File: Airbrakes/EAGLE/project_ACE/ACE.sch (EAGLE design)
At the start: 4 parts, among them J3 PTH

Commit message: Update ACE.sch
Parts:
- added 0OHM: (no value), fab_new:R1206
- added PAD1, PAD2: (no value), wirepad:2,15/1,0
- added POWER_TERMINAL: CONN_02_TERM-ADAFRUIT, fab_new:CONN_02_TERM-ADAFRUIT
- added R1, R2: 0 ohm, fab_new:R1206
- added SERVO_TERMINAL: CONN_03_TERM'-FABLAB', fab_new:CONN_03_TERM'-FABLAB'
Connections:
- new net 7.4V: POWER_TERMINAL.2, SERVO_TERMINAL.3
- new net N$2: R1.2, R2.1
- new net PWM: 0OHM.1, 0OHM.2, SERVO_TERMINAL.1, U$10.PWM_7
- net GND: now also PAD1.P, PAD2.P, POWER_TERMINAL.1, R2.2, SERVO_TERMINAL.2
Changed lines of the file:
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@@
 <layers>
 <layer number="1" name="Top" color="4" fill="1" visible="no" active="no"/>
+<layer number="2" name="Route2" color="1" fill="3" visible="no" active="no"/>
+<layer number="3" name="Route3" color="4" fill="3" visible="no" active="no"/>
+<layer number="4" name="Route4" color="1" fill="4" visible="no" active="no"/>
+<layer number="5" name="Route5" color="4" fill="4" visible="no" active="no"/>
+<layer number="6" name="Route6" color="1" fill="8" visible="no" active="no"/>
+<layer number="7" name="Route7" color="4" fill="8" visible="no" active="no"/>
+<layer number="8" name="Route8" color="1" fill="2" visible="no" active="no"/>
+<layer number="9" name="Route9" color="4" fill="2" visible="no" active="no"/>
+<layer number="10" name="Route10" color="1" fill="7" visible="no" active="no"/>
+<layer number="11" name="Route11" color="4" fill="7" visible="no" active="no"/>
+<layer number="12" name="Route12" color="1" fill="5" visible="no" active="no"/>
+<layer number="13" name="Route13" color="4" fill="5" visible="no" active="no"/>
+<layer number="14" name="Route14" color="1" fill="6" visible="no" active="no"/>
+<layer number="15" name="Route15" color="4" fill="6" visible="no" active="no"/>
 <layer number="16" name="Bottom" color="1" fill="1" visible="no" active="no"/>
 <layer number="17" name="Pads" color="2" fill="1" visible="no" active="no"/>
@@
 <part name="P+1" library="supply1" library_urn="urn:adsk.eagle:library:371" deviceset="VCC" device=""/>
 <part name="U$12" library="microbuilder" deviceset="GND" device=""/>
+<part name="R1" library="fab_new" deviceset="R" device="1206" value="0 ohm"/>
+<part name="R2" library="fab_new" deviceset="R" device="1206" value="0 ohm"/>
+<part name="POWER_TERMINAL" library="fab_new" deviceset="CONN_02_TERM" device="-ADAFRUIT"/>
+<part name="SERVO_TERMINAL" library="fab_new" deviceset="CONN_03_TERM" device="'-FABLAB'"/>
+<part name="0OHM" library="fab_new" deviceset="R" device="1206"/>
+<part name="PAD1" library="wirepad" library_urn="urn:adsk.eagle:library:412" deviceset="2,15/1,0" device="" package3d_urn="urn:adsk.eagle:package:30831/1"/>
+<part name="PAD2" library="wirepad" library_urn="urn:adsk.eagle:library:412" deviceset="2,15/1,0" device="" package3d_urn="urn:adsk.eagle:package:30831/1"/>
 </parts>
 <sheets>
@@
 <attribute name="VALUE" x="39.116" y="55.88" size="1.27" layer="96"/>
 </instance>
+<instance part="R1" gate="G$1" x="35.56" y="2.54" smashed="yes">
+<attribute name="NAME" x="31.75" y="4.0386" size="1.778" layer="95"/>
+<attribute name="VALUE" x="31.75" y="-0.762" size="1.778" layer="96"/>
+</instance>
+<instance part="R2" gate="G$1" x="45.72" y="2.54" smashed="yes">
+<attribute name="NAME" x="41.91" y="4.0386" size="1.778" layer="95"/>
+<attribute name="VALUE" x="41.91" y="-0.762" size="1.778" layer="96"/>
+</instance>
+<instance part="POWER_TERMINAL" gate="G$1" x="53.34" y="55.88" smashed="yes" rot="R90">
+<attribute name="NAME" x="47.625" y="53.34" size="1.778" layer="95" rot="R90"/>
+</instance>
+<instance part="SERVO_TERMINAL" gate="G$1" x="53.34" y="45.72" smashed="yes" rot="R90">
+<attribute name="NAME" x="47.625" y="43.18" size="1.778" layer="95" rot="R90"/>
+</instance>
+<instance part="0OHM" gate="G$1" x="-5.08" y="33.02" smashed="yes">
+<attribute name="NAME" x="-8.89" y="34.5186" size="1.778" layer="95"/>
+<attribute name="VALUE" x="-8.89" y="29.718" size="1.778" layer="96"/>
+</instance>
+<instance part="PAD1" gate="1" x="48.26" y="15.24" smashed="yes">
+<attribute name="NAME" x="47.117" y="17.0942" size="1.778" layer="95"/>
+<attribute name="VALUE" x="47.117" y="11.938" size="1.778" layer="96"/>
+</instance>
+<instance part="PAD2" gate="1" x="50.8" y="0" smashed="yes" rot="R90">
+<attribute name="NAME" x="48.9458" y="-1.143" size="1.778" layer="95" rot="R90"/>
+<attribute name="VALUE" x="54.102" y="-1.143" size="1.778" layer="96" rot="R90"/>
+</instance>
 </instances>
 <busses>
@@
 <wire x1="71.12" y1="17.78" x2="71.12" y2="15.24" width="0.1524" layer="91"/>
 <pinref part="GND12" gate="1" pin="GND"/>
+<pinref part="R2" gate="G$1" pin="2"/>
+<wire x1="71.12" y1="15.24" x2="50.8" y2="15.24" width="0.1524" layer="91"/>
+<wire x1="50.8" y1="15.24" x2="50.8" y2="2.54" width="0.1524" layer="91"/>
+<junction x="71.12" y="15.24"/>
+<pinref part="PAD1" gate="1" pin="P"/>
+<junction x="50.8" y="15.24"/>
+<pinref part="PAD2" gate="1" pin="P"/>
+<junction x="50.8" y="2.54"/>
 </segment>
 <segment>
@@
 <wire x1="35.56" y1="60.96" x2="40.64" y2="60.96" width="0.1524" layer="91"/>
 <pinref part="U$10" gate="G$1" pin="GND"/>
+<wire x1="40.64" y1="60.96" x2="40.64" y2="55.88" width="0.1524" layer="91"/>
+<junction x="40.64" y="60.96"/>
+<pinref part="POWER_TERMINAL" gate="G$1" pin="1"/>
+<wire x1="40.64" y1="55.88" x2="50.8" y2="55.88" width="0.1524" layer="91"/>
+<pinref part="SERVO_TERMINAL" gate="G$1" pin="2"/>
+<wire x1="53.34" y1="45.72" x2="53.34" y2="53.34" width="0.1524" layer="91"/>
+<wire x1="53.34" y1="53.34" x2="50.8" y2="53.34" width="0.1524" layer="91"/>
+<wire x1="50.8" y1="53.34" x2="50.8" y2="55.88" width="0.1524" layer="91"/>
+<junction x="50.8" y="55.88"/>
 </segment>
 </net>
@@
 <pinref part="U$1" gate="G$1" pin="GND_1"/>
 <wire x1="165.1" y1="53.34" x2="175.26" y2="53.34" width="0.1524" layer="91"/>
+</segment>
+</net>
+<net name="N$2" class="0">
+<segment>
+<pinref part="R1" gate="G$1" pin="2"/>
+<pinref part="R2" gate="G$1" pin="1"/>
+</segment>
+</net>
+<net name="7.4V" class="0">
+<segment>
+<pinref part="POWER_TERMINAL" gate="G$1" pin="2"/>
+<pinref part="SERVO_TERMINAL" gate="G$1" pin="3"/>
+<wire x1="53.34" y1="55.88" x2="55.88" y2="55.88" width="0.1524" layer="91"/>
+<wire x1="55.88" y1="55.88" x2="55.88" y2="45.72" width="0.1524" layer="91"/>
+</segment>
+</net>
+<net name="PWM" class="0">
+<segment>
+<pinref part="0OHM" gate="G$1" pin="1"/>
+<wire x1="-10.16" y1="33.02" x2="-10.16" y2="27.94" width="0.1524" layer="91"/>
+<wire x1="-10.16" y1="27.94" x2="0" y2="27.94" width="0.1524" layer="91"/>
+<pinref part="SERVO_TERMINAL" gate="G$1" pin="1"/>
+<wire x1="0" y1="27.94" x2="50.8" y2="27.94" width="0.1524" layer="91"/>
+<wire x1="53.34" y1="27.94" x2="50.8" y2="27.94" width="0.1524" layer="91"/>
+<wire x1="50.8" y1="27.94" x2="50.8" y2="45.72" width="0.1524" layer="91"/>
+<pinref part="U$10" gate="G$1" pin="PWM_7"/>
+<pinref part="0OHM" gate="G$1" pin="2"/>
+<wire x1="0" y1="33.02" x2="0" y2="27.94" width="0.1524" layer="91"/>
+<junction x="0" y="33.02"/>
+<junction x="0" y="27.94"/>
 </segment>
 </net>
@@
 will not be understood (or retained) with this version.
 </note>
+<note version="8.3" severity="warning">
+Since Version 8.3, EAGLE supports the association of 3D packages
+with devices in libraries, schematics, and board files. Those 3D
+packages will not be understood (or retained) with this version.
+</note>
 </compatibility>

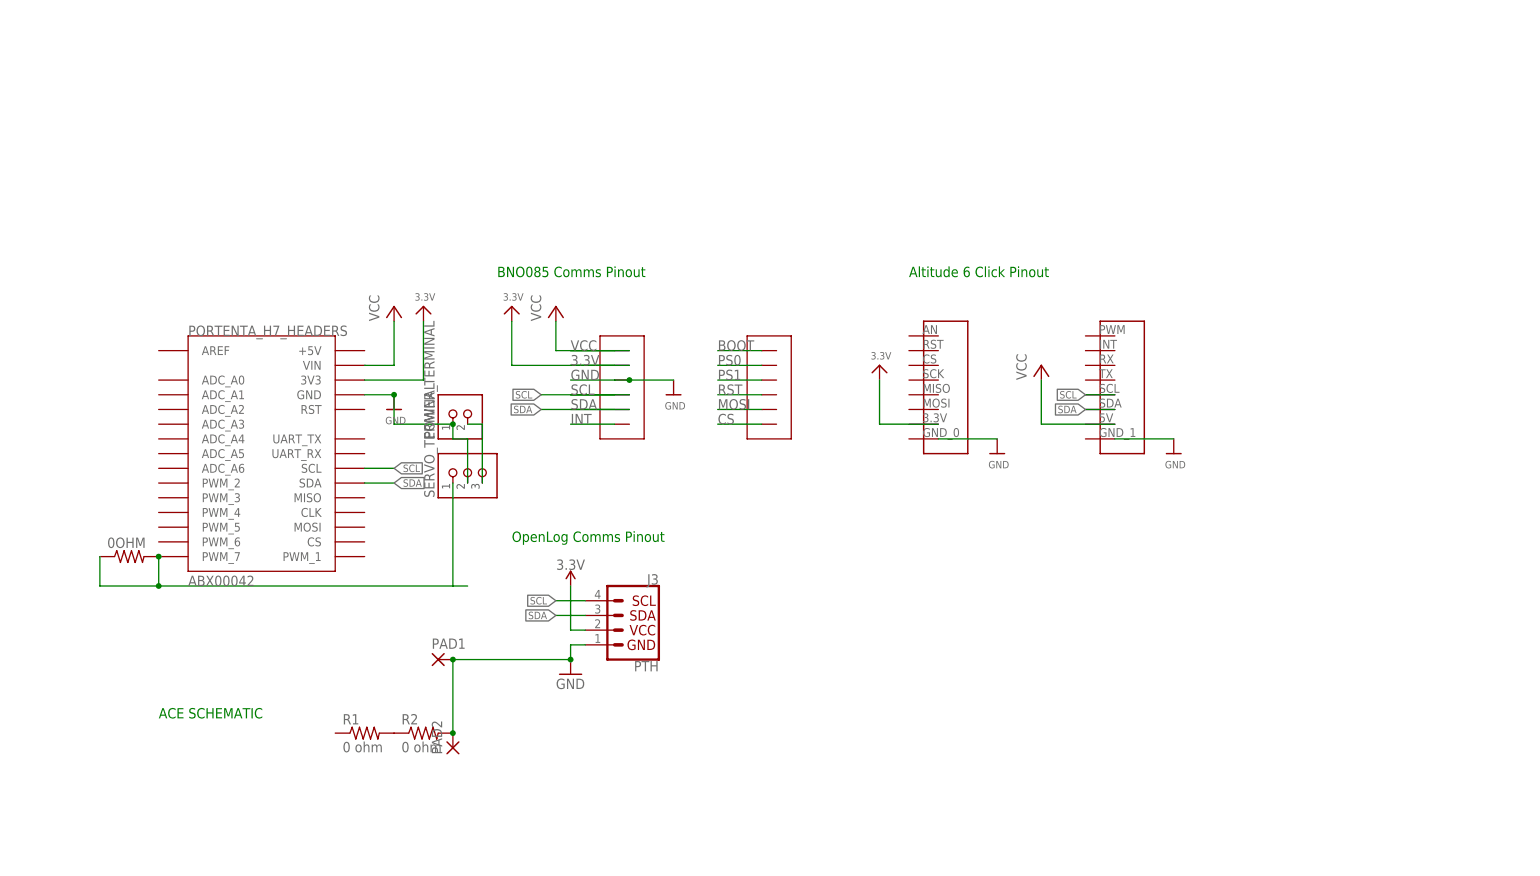
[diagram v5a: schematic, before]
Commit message: Reroute layout and schematic
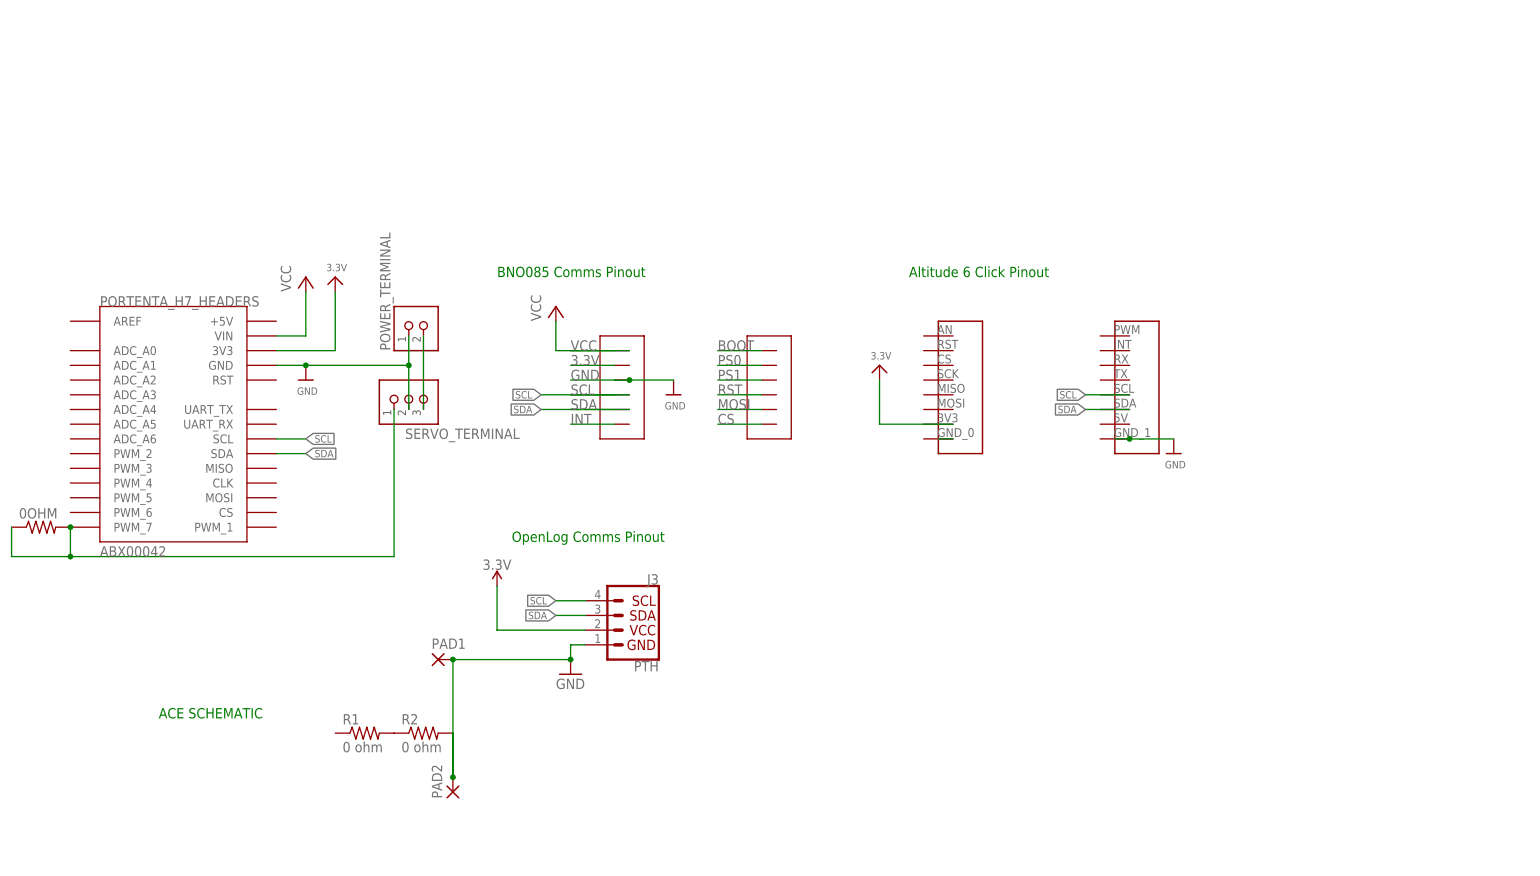
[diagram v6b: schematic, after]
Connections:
- removed net N$1: U$1.GND_1
- new net N$4: U$1.GND_0
- net 3.3V: no longer U$5.3.3V
- net GND: now also U$1.GND_1; no longer U$1.GND_0
- net VCC: no longer U$1.5V
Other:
- moved on the sheet: 0OHM, PAD2, POWER_TERMINAL, SERVO_TERMINAL

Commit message: ACE PCB updates
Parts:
- removed PAD1, PAD2: (no value), wirepad:2,15/1,0
- removed R1, R2: 0 ohm, fab_new:R1206
- added ROTARY_TERMINAL: CONN_02_TERM-ADAFRUIT, fab_new:CONN_02_TERM-ADAFRUIT
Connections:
- removed net N$2: R1.2, R2.1
- net GND: now also ROTARY_TERMINAL.1, ROTARY_TERMINAL.2; no longer PAD1.P, PAD2.P, R2.2
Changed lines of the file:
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@@
 <part name="P+1" library="supply1" library_urn="urn:adsk.eagle:library:371" deviceset="VCC" device=""/>
 <part name="U$12" library="microbuilder" deviceset="GND" device=""/>
-<part name="R1" library="fab_new" deviceset="R" device="1206" value="0 ohm"/>
-<part name="R2" library="fab_new" deviceset="R" device="1206" value="0 ohm"/>
 <part name="POWER_TERMINAL" library="fab_new" deviceset="CONN_02_TERM" device="-ADAFRUIT"/>
 <part name="SERVO_TERMINAL" library="fab_new" deviceset="CONN_03_TERM" device="'-FABLAB'"/>
 <part name="0OHM" library="fab_new" deviceset="R" device="1206"/>
-<part name="PAD1" library="wirepad" library_urn="urn:adsk.eagle:library:412" deviceset="2,15/1,0" device="" package3d_urn="urn:adsk.eagle:package:30831/1"/>
-<part name="PAD2" library="wirepad" library_urn="urn:adsk.eagle:library:412" deviceset="2,15/1,0" device="" package3d_urn="urn:adsk.eagle:package:30831/1"/>
 <part name="U$1" library="MIKROE-4903" deviceset="MIKROE-ALTITUDE-6-CLICK-DVC" device=""/>
+<part name="ROTARY_TERMINAL" library="fab_new" deviceset="CONN_02_TERM" device="-ADAFRUIT"/>
 </parts>
 <sheets>
@@
 <attribute name="VALUE" x="23.876" y="60.96" size="1.27" layer="96"/>
 </instance>
-<instance part="R1" gate="G$1" x="35.56" y="2.54" smashed="yes">
-<attribute name="NAME" x="31.75" y="4.0386" size="1.778" layer="95"/>
-<attribute name="VALUE" x="31.75" y="-0.762" size="1.778" layer="96"/>
-</instance>
-<instance part="R2" gate="G$1" x="45.72" y="2.54" smashed="yes">
-<attribute name="NAME" x="41.91" y="4.0386" size="1.778" layer="95"/>
-<attribute name="VALUE" x="41.91" y="-0.762" size="1.778" layer="96"/>
-</instance>
 <instance part="POWER_TERMINAL" gate="G$1" x="45.72" y="71.12" smashed="yes" rot="R90">
 <attribute name="NAME" x="40.005" y="68.58" size="1.778" layer="95" rot="R90"/>
@@
 <attribute name="VALUE" x="-24.13" y="34.798" size="1.778" layer="96"/>
 </instance>
-<instance part="PAD1" gate="1" x="48.26" y="15.24" smashed="yes">
-<attribute name="NAME" x="47.117" y="17.0942" size="1.778" layer="95"/>
-<attribute name="VALUE" x="47.117" y="11.938" size="1.778" layer="96"/>
-</instance>
-<instance part="PAD2" gate="1" x="50.8" y="-7.62" smashed="yes" rot="R90">
-<attribute name="NAME" x="48.9458" y="-8.763" size="1.778" layer="95" rot="R90"/>
-<attribute name="VALUE" x="54.102" y="-8.763" size="1.778" layer="96" rot="R90"/>
-</instance>
 <instance part="U$1" gate="G$1" x="134.62" y="50.8" smashed="yes"/>
+<instance part="ROTARY_TERMINAL" gate="G$1" x="68.58" y="2.54" smashed="yes" rot="R270">
+<attribute name="NAME" x="74.295" y="5.08" size="1.778" layer="95" rot="R270"/>
+</instance>
 </instances>
 <busses>
@@
 <wire x1="71.12" y1="17.78" x2="71.12" y2="15.24" width="0.1524" layer="91"/>
 <pinref part="GND12" gate="1" pin="GND"/>
-<pinref part="R2" gate="G$1" pin="2"/>
-<wire x1="71.12" y1="15.24" x2="50.8" y2="15.24" width="0.1524" layer="91"/>
-<wire x1="50.8" y1="15.24" x2="50.8" y2="-5.08" width="0.1524" layer="91"/>
+<pinref part="ROTARY_TERMINAL" gate="G$1" pin="2"/>
+<pinref part="ROTARY_TERMINAL" gate="G$1" pin="1"/>
+<wire x1="68.58" y1="2.54" x2="71.12" y2="2.54" width="0.1524" layer="91"/>
+<wire x1="71.12" y1="15.24" x2="71.12" y2="2.54" width="0.1524" layer="91"/>
 <junction x="71.12" y="15.24"/>
-<pinref part="PAD1" gate="1" pin="P"/>
-<junction x="50.8" y="15.24"/>
-<pinref part="PAD2" gate="1" pin="P"/>
-<junction x="50.8" y="-5.08"/>
-<wire x1="50.8" y1="-5.08" x2="50.8" y2="2.54" width="0.1524" layer="91"/>
+<junction x="71.12" y="2.54"/>
 </segment>
 <segment>
@@
 <label x="25.4" y="50.8" size="1.27" layer="95" xref="yes"/>
 <pinref part="U$10" gate="G$1" pin="SDA"/>
-</segment>
-</net>
-<net name="N$2" class="0">
-<segment>
-<pinref part="R1" gate="G$1" pin="2"/>
-<pinref part="R2" gate="G$1" pin="1"/>
 </segment>
 </net>
@@
 will not be understood (or retained) with this version.
 </note>
-<note version="8.3" severity="warning">
-Since Version 8.3, EAGLE supports the association of 3D packages
-with devices in libraries, schematics, and board files. Those 3D
-packages will not be understood (or retained) with this version.
-</note>
 </compatibility>

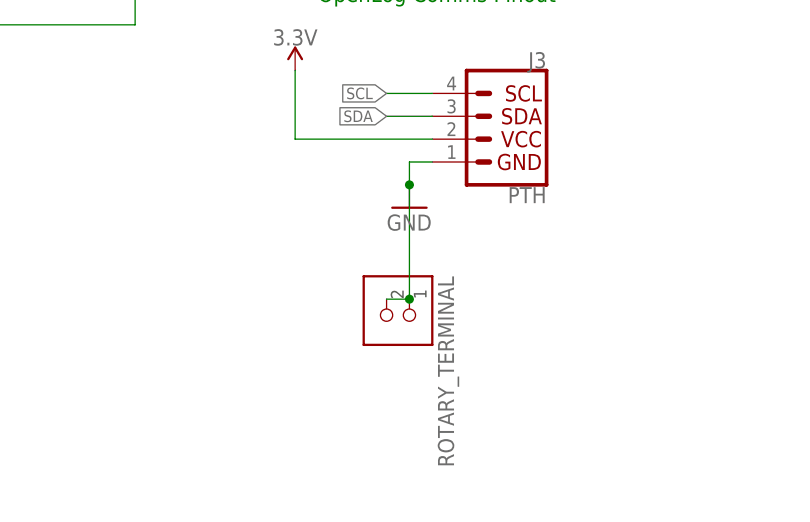
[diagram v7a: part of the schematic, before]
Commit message: change terminals on ACE PCB to 200mil pitch
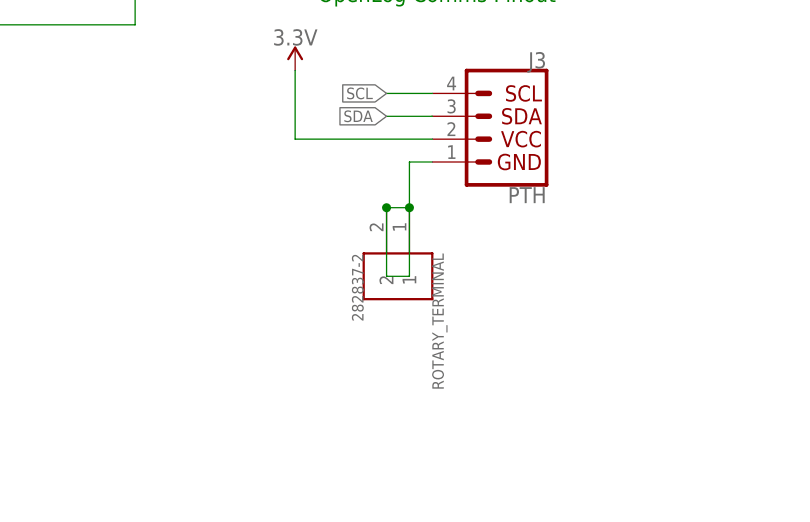
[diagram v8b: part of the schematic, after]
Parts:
- ROTARY_TERMINAL: value CONN_02_TERM-ADAFRUIT -> 282837-2; device fab_new:CONN_02_TERM-ADAFRUIT -> 282837-2:282837-2
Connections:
- new net N$2: J3.GND, ROTARY_TERMINAL.1, ROTARY_TERMINAL.2
- net GND: no longer J3.GND, ROTARY_TERMINAL.1, ROTARY_TERMINAL.2
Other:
- moved on the sheet: ROTARY_TERMINAL
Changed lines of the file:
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@@
 <part name="SUPPLY7" library="SparkFun-PowerSymbols" deviceset="3.3V" device=""/>
 <part name="J3" library="SparkX" deviceset="I2C_STANDARD" device="_NO_SILK" value="PTH"/>
-<part name="GND12" library="SparkFun" deviceset="GND" device=""/>
 <part name="U$3" library="microbuilder" deviceset="GND" device=""/>
 <part name="U$4" library="microbuilder" deviceset="3.3V" device=""/>
@@
 <part name="0OHM" library="fab_new" deviceset="R" device="1206"/>
 <part name="U$1" library="MIKROE-4903" deviceset="MIKROE-ALTITUDE-6-CLICK-DVC" device=""/>
-<part name="ROTARY_TERMINAL" library="fab_new" deviceset="CONN_02_TERM" device="-ADAFRUIT"/>
+<part name="ROTARY_TERMINAL" library="282837-2" deviceset="282837-2" device=""/>
 </parts>
 <sheets>
@@
 <attribute name="NAME" x="86.36" y="28.194" size="1.778" layer="95" font="vector" rot="MR0"/>
 </instance>
-<instance part="GND12" gate="1" x="71.12" y="12.7" smashed="yes">
-<attribute name="VALUE" x="68.58" y="10.16" size="1.778" layer="96"/>
-</instance>
 <instance part="U$3" gate="G$1" x="175.26" y="50.8" smashed="yes">
 <attribute name="VALUE" x="173.736" y="48.26" size="1.27" layer="96"/>
@@
 </instance>
 <instance part="U$1" gate="G$1" x="134.62" y="50.8" smashed="yes"/>
-<instance part="ROTARY_TERMINAL" gate="G$1" x="68.58" y="2.54" smashed="yes" rot="R270">
-<attribute name="NAME" x="74.295" y="5.08" size="1.778" layer="95" rot="R270"/>
+<instance part="ROTARY_TERMINAL" gate="G$1" x="71.12" y="5.08" smashed="yes" rot="R270">
+<attribute name="NAME" x="73.66381875" y="7.620559375" size="1.271909375" layer="95" rot="R270"/>
+<attribute name="VALUE" x="64.745490625" y="7.62236875" size="1.274909375" layer="96" rot="R270"/>
 </instance>
 </instances>
@@
 <nets>
 <net name="GND" class="2">
-<segment>
-<pinref part="J3" gate="G$1" pin="GND"/>
-<wire x1="73.66" y1="17.78" x2="71.12" y2="17.78" width="0.1524" layer="91"/>
-<wire x1="71.12" y1="17.78" x2="71.12" y2="15.24" width="0.1524" layer="91"/>
-<pinref part="GND12" gate="1" pin="GND"/>
-<pinref part="ROTARY_TERMINAL" gate="G$1" pin="2"/>
-<pinref part="ROTARY_TERMINAL" gate="G$1" pin="1"/>
-<wire x1="68.58" y1="2.54" x2="71.12" y2="2.54" width="0.1524" layer="91"/>
-<wire x1="71.12" y1="15.24" x2="71.12" y2="2.54" width="0.1524" layer="91"/>
-<junction x="71.12" y="15.24"/>
-<junction x="71.12" y="2.54"/>
-</segment>
 <segment>
 <pinref part="U$7" gate="G$1" pin="GND"/>
@@
 </segment>
 </net>
+<net name="N$2" class="2">
+<segment>
+<pinref part="J3" gate="G$1" pin="GND"/>
+<wire x1="73.66" y1="17.78" x2="71.12" y2="17.78" width="0.1524" layer="91"/>
+<pinref part="ROTARY_TERMINAL" gate="G$1" pin="1"/>
+<wire x1="71.12" y1="17.78" x2="71.12" y2="12.7" width="0.1524" layer="91"/>
+<pinref part="ROTARY_TERMINAL" gate="G$1" pin="2"/>
+<wire x1="71.12" y1="12.7" x2="68.58" y2="12.7" width="0.1524" layer="91"/>
+<junction x="71.12" y="12.7"/>
+<wire x1="71.12" y1="12.7" x2="71.12" y2="5.08" width="0.1524" layer="91"/>
+<wire x1="71.12" y1="5.08" x2="68.58" y2="5.08" width="0.1524" layer="91"/>
+<wire x1="68.58" y1="5.08" x2="68.58" y2="12.7" width="0.1524" layer="91"/>
+<junction x="68.58" y="12.7"/>
+</segment>
+</net>
